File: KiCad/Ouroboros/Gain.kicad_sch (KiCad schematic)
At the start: 7 parts, among them U1 Opamp_Quad

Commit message: Updating schematic
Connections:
- net IN_GAIN: now reaches D1.2 (A), D2.1 (K), RV1.3, U1.7
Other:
- note added: "Gain Stage"
- note added: "[3] Gain"
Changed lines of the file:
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@@
+		)
+	)
+	(polyline
+		(pts
+			(xy 96.52 59.69) (xy 205.74 59.69)
+		)
+		(stroke
+			(width 0)
+			(type default)
 		)
 	)
@@
 		)
 	)
+	(polyline
+		(pts
+			(xy 205.74 124.46) (xy 205.74 59.69)
+		)
+		(stroke
+			(width 0)
+			(type default)
+		)
+	)
 	(wire
 		(pts
@@
 		)
 	)
+	(polyline
+		(pts
+			(xy 96.52 59.69) (xy 96.52 124.46)
+		)
+		(stroke
+			(width 0)
+			(type default)
+		)
+	)
 	(wire
 		(pts
@@
 			(width 0)
 			(type default)
+		)
+	)
+	(polyline
+		(pts
+			(xy 96.52 124.46) (xy 205.74 124.46)
+		)
+		(stroke
+			(width 0)
+			(type default)
+		)
+	)
+	(text "Gain Stage"
+		(exclude_from_sim no)
+		(at 152.4 65.024 0)
+		(effects
+			(font
+				(size 5 5)
+			)
+		)
+	)
+	(text "[3] Gain"
+		(exclude_from_sim no)
+		(at 151.892 19.558 0)
+		(effects
+			(font
+				(size 5 5)
+				(color 132 0 0 1)
+			)
 		)
 	)
@@
 		(fields_autoplaced yes)
 		(effects
+			(font
+				(size 1.27 1.27)
+			)
+			(justify left bottom)
+		)
+	)
+	(label "IN_GAIN"
+		(at 186.69 81.28 0)
+		(fields_autoplaced yes)
+		(effects

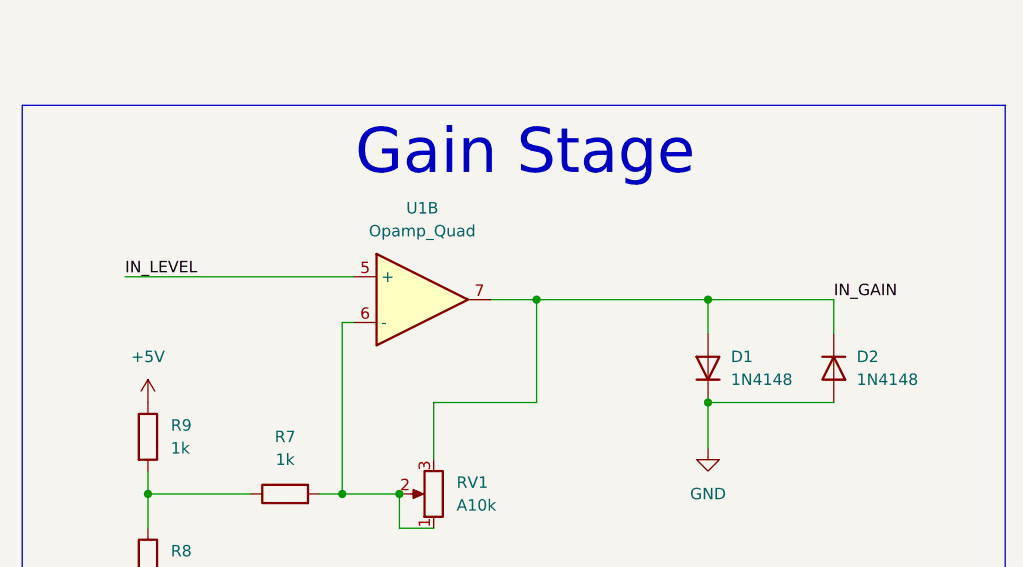
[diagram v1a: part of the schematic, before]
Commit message: Linking nets
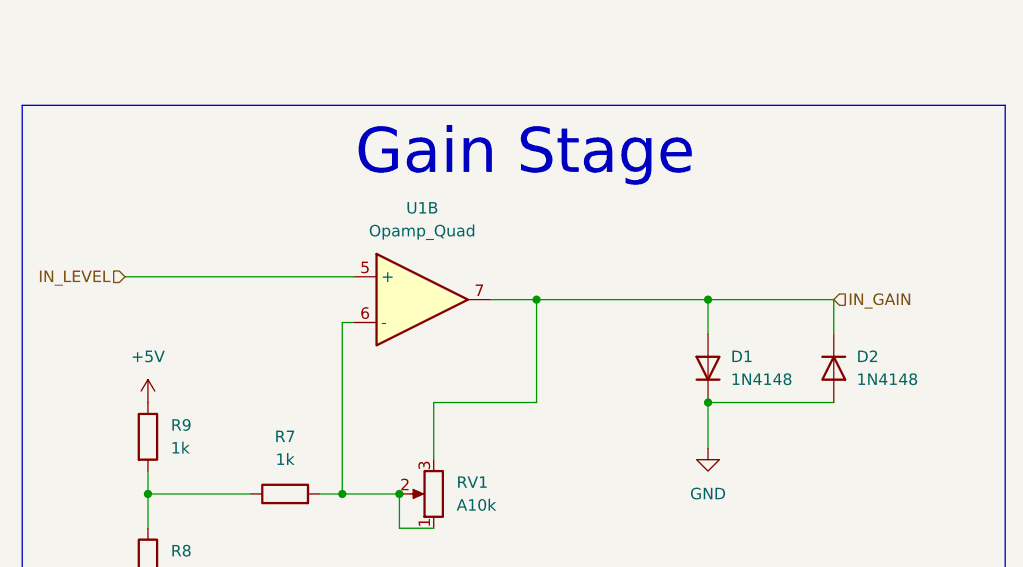
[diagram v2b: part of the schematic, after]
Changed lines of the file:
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@@
 		)
 	)
-	(label "IN_LEVEL"
-		(at 107.95 78.74 0)
-		(fields_autoplaced yes)
-		(effects
-			(font
-				(size 1.27 1.27)
-			)
-			(justify left bottom)
-		)
-	)
-	(label "IN_GAIN"
+	(hierarchical_label "IN_GAIN"
+		(shape input)
 		(at 186.69 81.28 0)
 		(fields_autoplaced yes)
@@
 				(size 1.27 1.27)
 			)
-			(justify left bottom)
+			(justify left)
 		)
 	)
+	(hierarchical_label "IN_LEVEL"
+		(shape input)
+		(at 107.95 78.74 180)
+		(fields_autoplaced yes)
+		(effects
+			(font
+				(size 1.27 1.27)
+			)
+			(justify right)
+		)
+	)

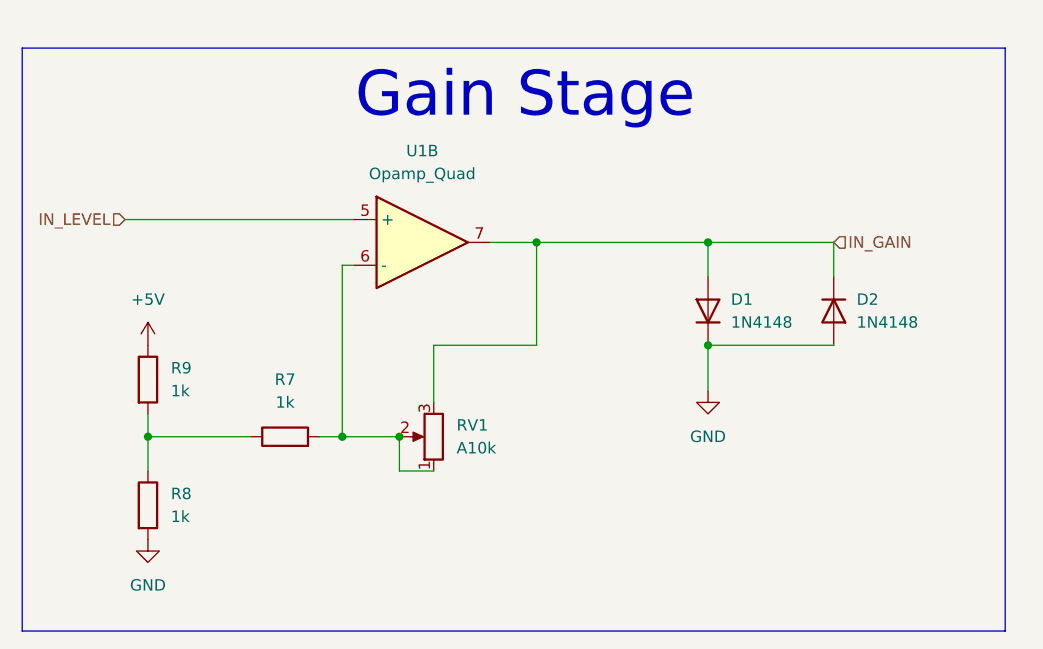
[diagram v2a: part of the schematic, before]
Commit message: Updated schematic, started PCB
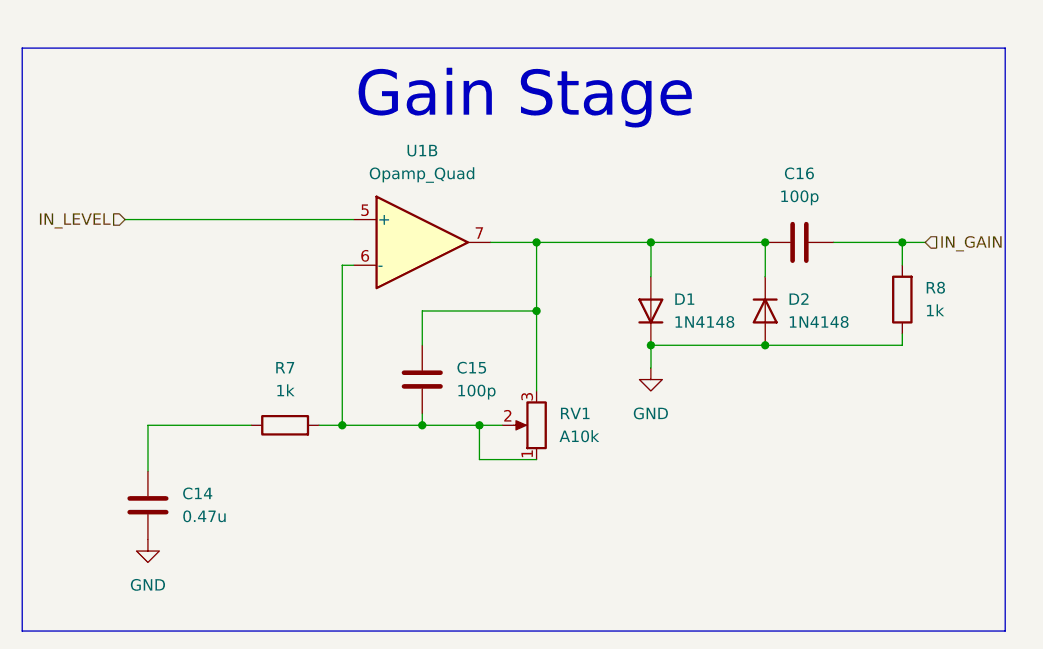
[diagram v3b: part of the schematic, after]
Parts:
- removed R9: 1k, symbol Device:R
- added C14: 0.47u, Capacitor_THT:C_Rect_L7.0mm_W3.5mm_P5.00mm, symbol Device:C
- added C15, C16: 100p, Capacitor_THT:C_Rect_L7.0mm_W3.5mm_P5.00mm, symbol Device:C
- R7, R8: footprint (none) -> Resistor_THT:R_Axial_DIN0207_L6.3mm_D2.5mm_P10.16mm_Horizontal
- RV1: footprint (none) -> Potentiometer_THT:Potentiometer_Alpha_RD901F-40-00D_Single_Vertical
- U1: footprint (none) -> Package_DIP:DIP-14_W7.62mm_Socket; symbol Device:Opamp_Quad -> Amplifier_Operational:TL074
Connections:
- net GND: now also R8.1, C14.2; no longer R8.2
- net IN_GAIN: now also R8.2, C16.2; no longer D1.2 (A), D2.1 (K), RV1.3, U1.7
- net at R7.1: now also C14.1; no longer R8.1
- net at R7.2, RV1.1, RV1.2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: now also C15.2
- new net: C15.1, C16.1, D1.2 (A), D2.1 (K), RV1.3, U1.7
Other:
- moved on the sheet: D1, D2, R7, RV1

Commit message: PCB Finished
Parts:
- C16: value 100p -> 1u; footprint Capacitor_THT:C_Rect_L7.0mm_W3.5mm_P5.00mm -> Capacitor_THT:C_Rect_L7.0mm_W6.0mm_P5.00mm
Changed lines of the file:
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@@
 			)
 		)
-		(property "Value" "100p"
+		(property "Value" "1u"
 			(at 182.88 76.2 90)
 			(effects
@@
 			)
 		)
-		(property "Footprint" "Capacitor_THT:C_Rect_L7.0mm_W3.5mm_P5.00mm"
+		(property "Footprint" "Capacitor_THT:C_Rect_L7.0mm_W6.0mm_P5.00mm"
 			(at 186.69 80.3148 0)
 			(effects

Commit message: Dev Board complete
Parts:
- added R28: 0R, Resistor_THT:R_Axial_DIN0204_L3.6mm_D1.6mm_P1.90mm_Vertical, symbol Device:R
- added R33, R34: 0R, Resistor_THT:R_Axial_DIN0207_L6.3mm_D2.5mm_P10.16mm_Horizontal, symbol Device:R
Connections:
- net IN_GAIN: now also R28.2; no longer C16.2, R8.2
- net at C15.1, C16.1, D1.2 (A)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: now also R33.2, R34.2
- net at C15.2, R7.2, RV1.1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: now also R33.1, R34.1
- new net: C16.2, R28.1, R8.2
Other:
- note added: "NF"
- moved on the sheet: RV1
